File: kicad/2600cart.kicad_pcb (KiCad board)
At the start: 2 copper layers, 4 parts, among them U1 2600Cartridge, U2 74LS04, U3 2732

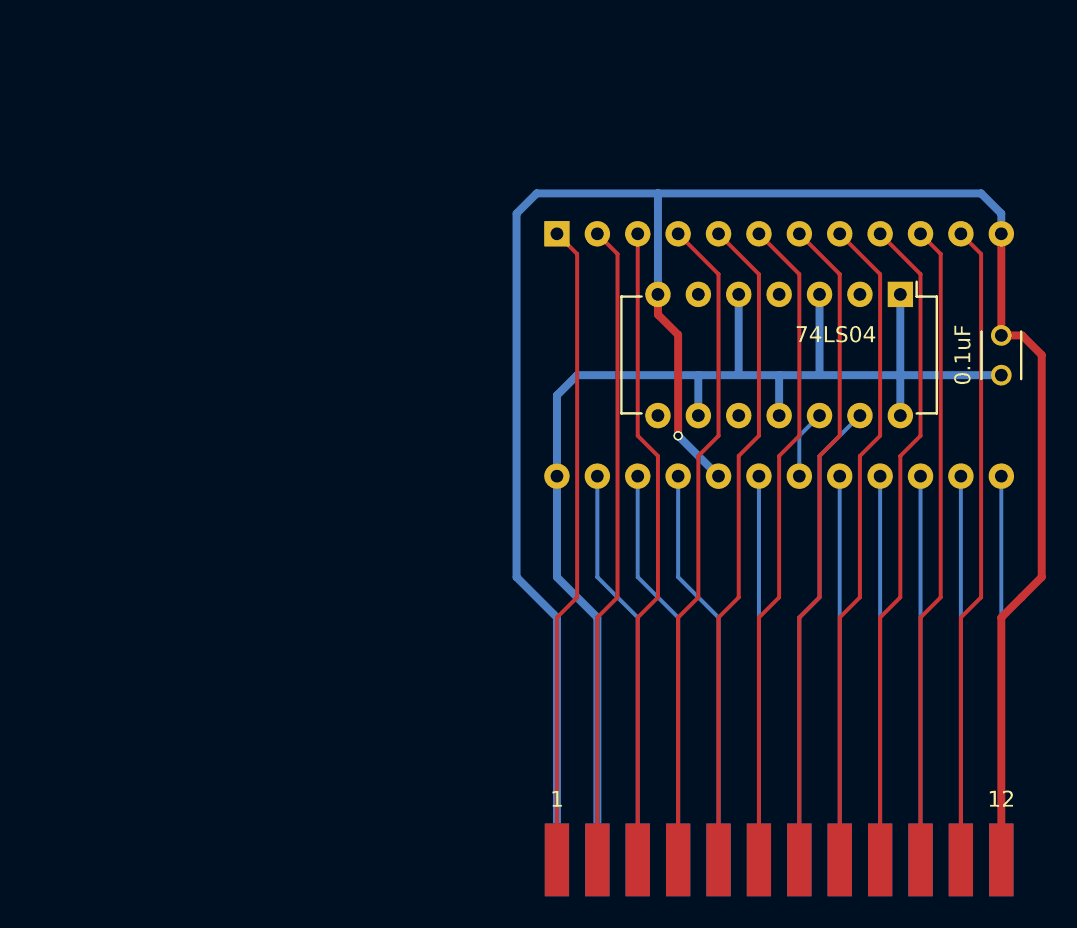
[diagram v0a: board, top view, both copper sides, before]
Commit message: MERGE all three project files
The schematic and netlist now directly map to the full cartridge PCB
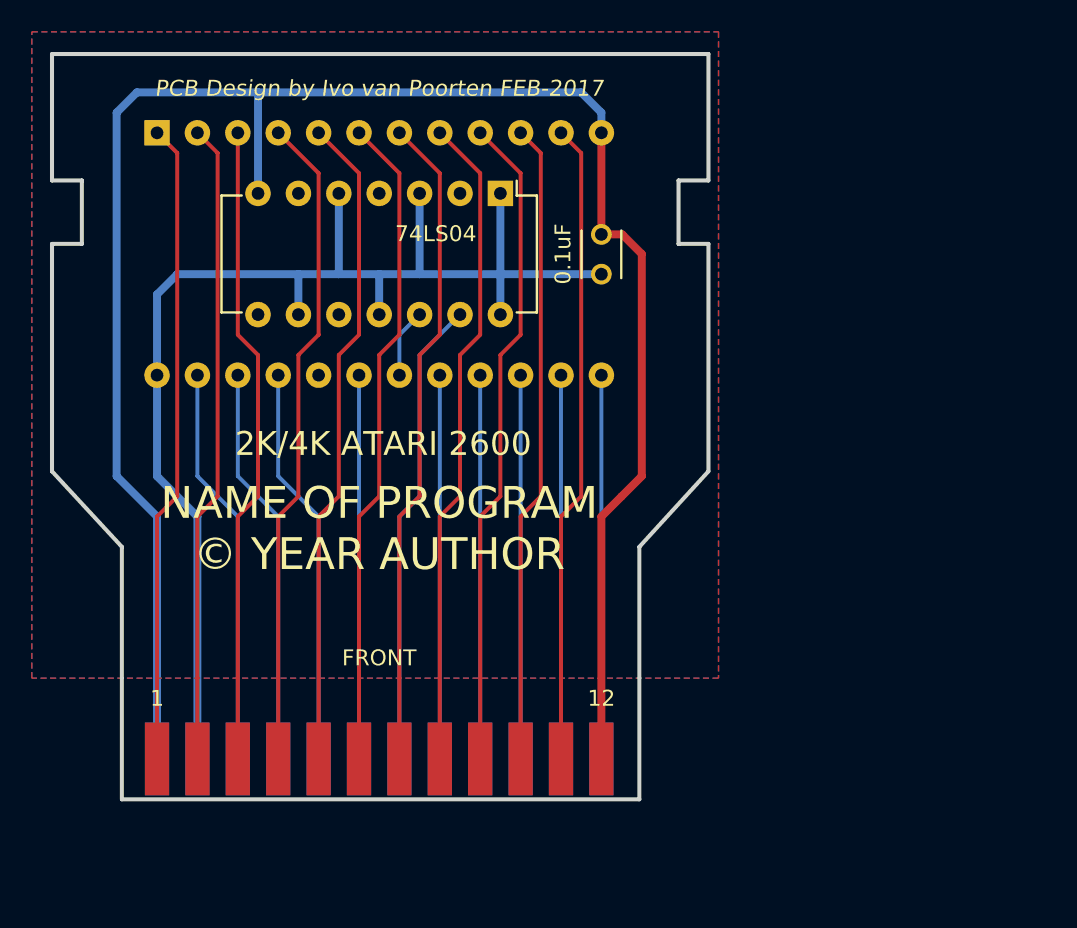
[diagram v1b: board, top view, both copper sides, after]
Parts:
- moved U2 25.9 mm to (117.1, 54.6)
- moved C1 25.9 mm to (123.4, 59.7)
- moved U1 25.9 mm to (109.5, 90.2)
- moved U3 25.9 mm to (95.5, 50.8)
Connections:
- U2 pad 10: Net-(U2-Pad10) -> (no net)
- U2 pad 2: Net-(U2-Pad2) -> (no net)
- U2 pad 4: Net-(U2-Pad4) -> (no net)
- U2 pad 6: Net-(U2-Pad6) -> (no net)
- U2 pad 8: Net-(U2-Pad8) -> (no net)
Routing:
- net GND: track 133.6 -> 120.5 mm, vias 1 -> 0
- added copper zone on B.Cu, net GND
- added copper zone on F.Cu, net GND
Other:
- board outline added: 41.3 x 46.9 mm
- board text added: "2K/4K ATARI 2600"
- board text added: "FRONT"
- board text added: "NAME OF PROGRAM © YEAR AUTHOR"
- board text added: "PCB Design by Ivo van Poorten FEB-2017"

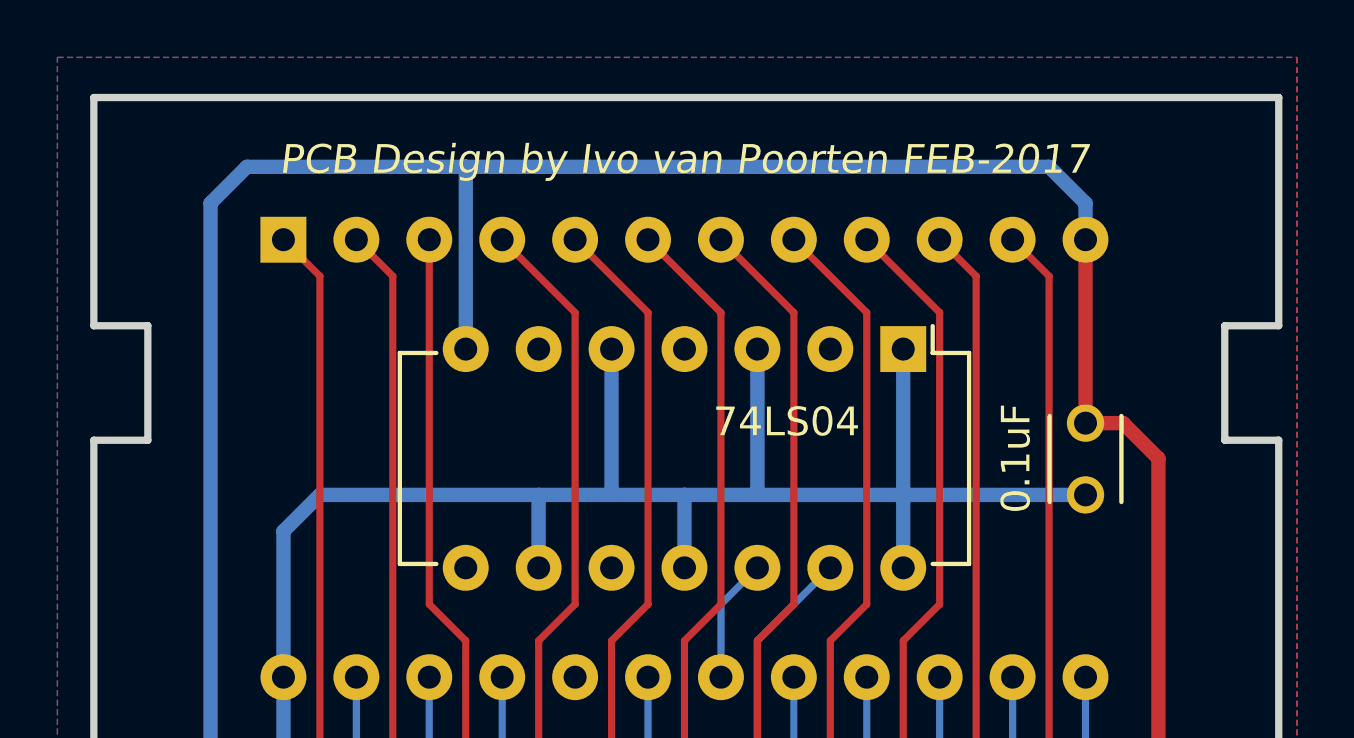
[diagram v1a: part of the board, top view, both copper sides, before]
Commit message: upgrade to new footprints and restore 3D rendering
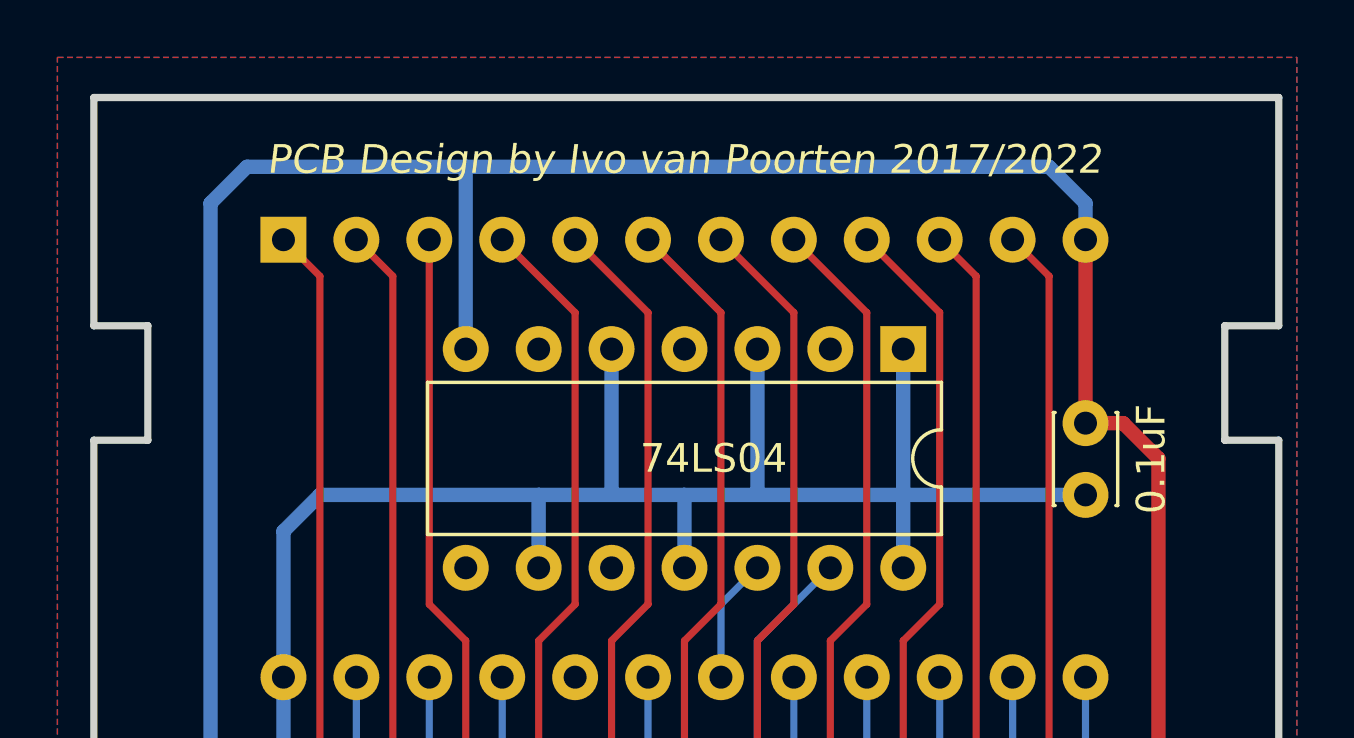
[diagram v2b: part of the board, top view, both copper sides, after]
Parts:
- C1: footprint Capacitors_ThroughHole:C_Disc_D3_P2.5 -> Capacitor_THT:C_Disc_D3.0mm_W2.0mm_P2.50mm
- U2: footprint Housings_DIP:DIP-14_W7.62mm -> Package_DIP:DIP-14_W7.62mm
- U3: footprint Housings_DIP:DIP-24_W15.24mm -> Package_DIP:DIP-24_W15.24mm
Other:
- board text added: "PCB Design by Ivo van Poorten 2017/2022"
- board text removed: "PCB Design by Ivo van Poorten FEB-2017"
